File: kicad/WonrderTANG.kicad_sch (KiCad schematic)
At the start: 28 parts, among them CON1 MSX-CONNECTOR, J2 AudioJack3, J3 Conn_02x01, Q1 2N3904, Q2 2N3904, U1 SN74LVC245AN, U2 SN74LVC245AN, U3 SN74LVC245AN, U4 SN74LVC245AN, U5 Tang_Nano_20k, U6 SN74LVC245AN

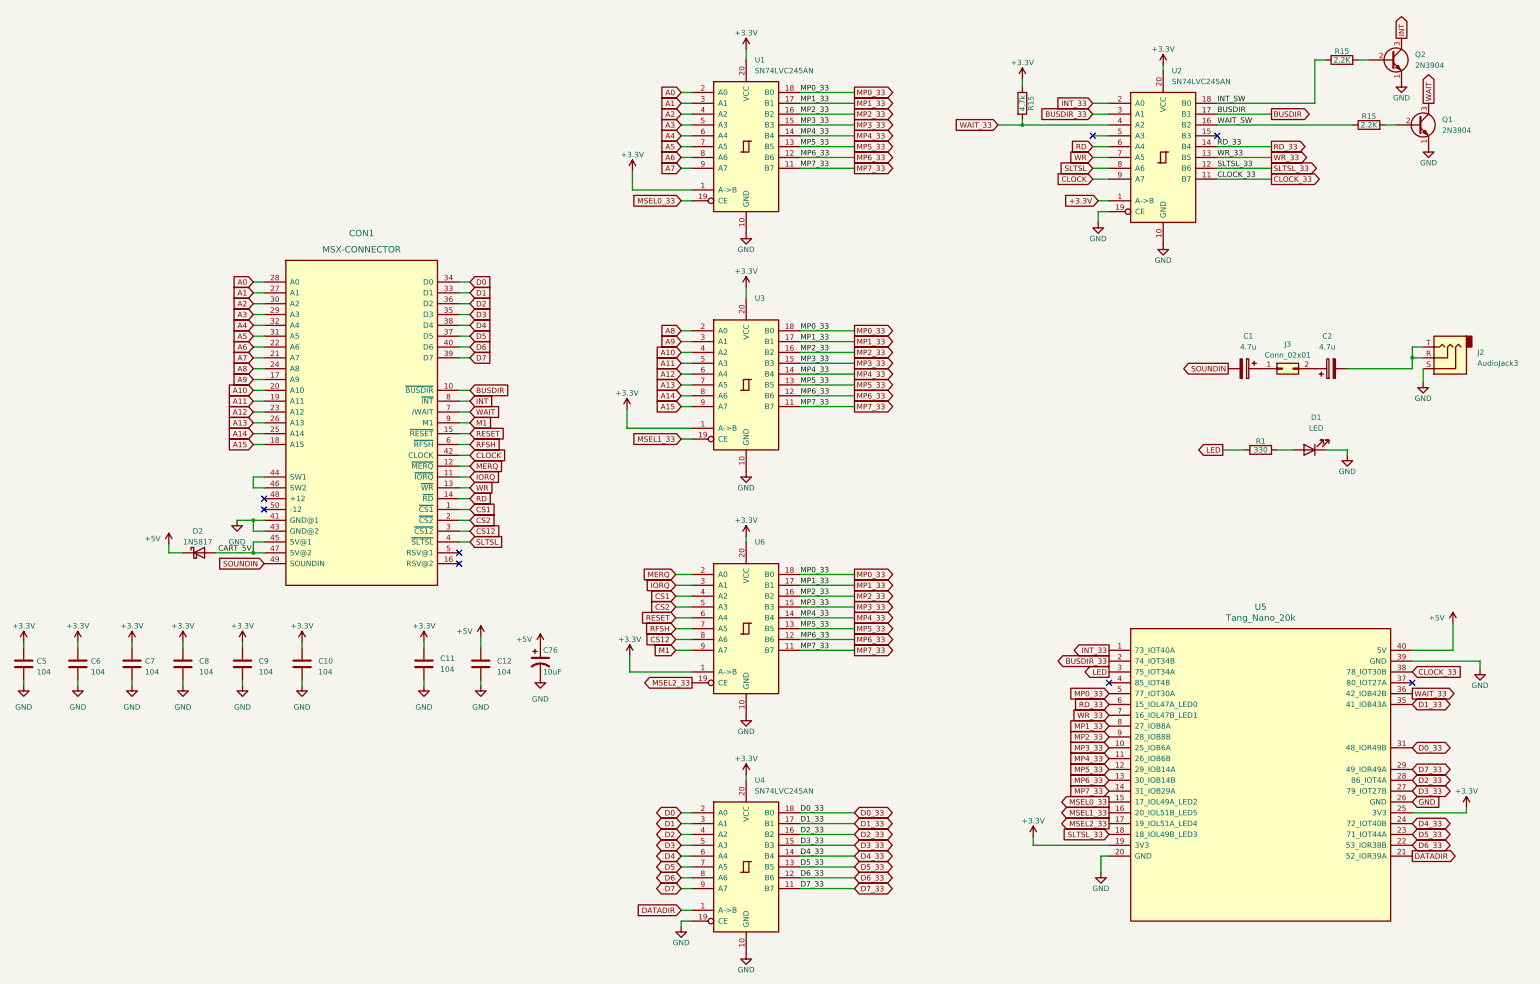
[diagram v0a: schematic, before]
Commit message: Version 2.0b RCC Rev1 - rotated J3 to better fit audio jumper
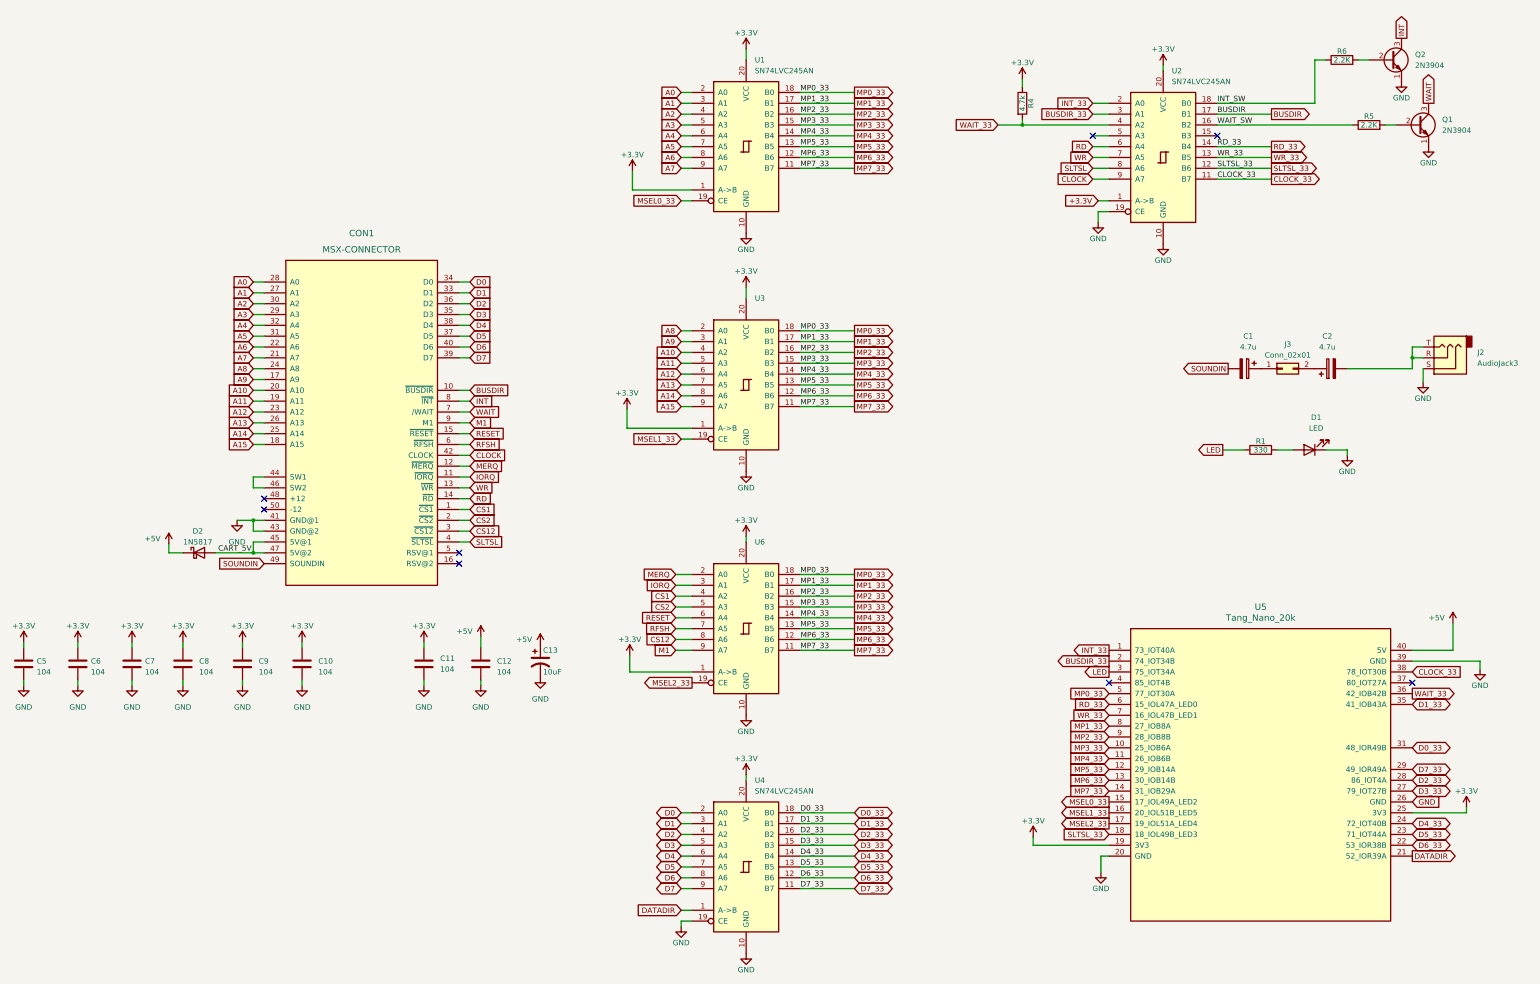
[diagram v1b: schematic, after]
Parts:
- J3: footprint Connector_PinHeader_2.54mm:PinHeader_2x01_P2.54mm_Vertical -> Connector_PinHeader_2.54mm:PinHeader_1x02_P2.54mm_Horizontal
- renumbered C76 to C13, R15 to R4, R15 to R5, R15 to R6
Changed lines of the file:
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@@
 (kicad_sch
-	(version 20231120)
+	(version 20250114)
 	(generator "eeschema")
-	(generator_version "8.0")
+	(generator_version "9.0")
 	(paper "A3")
 	(title_block
 		(title "MSX wonderTANG 2.0")
-		(date "2023-03-01")
+		(date "2025-05-26")
+		(rev "2.0b (RCC Rev 1)")
 	)
 	(junction
@@
 	(label "CART_5V"
 		(at 93.345 153.67 0)
-		(fields_autoplaced yes)
 		(effects
 			(font
@@
 	(label "D0_33"
 		(at 229.87 214.63 0)
-		(fields_autoplaced yes)
 		(effects
 			(font
@@
 	(label "MP5_33"
 		(at 229.87 171.45 0)
-		(fields_autoplaced yes)
 		(effects
 			(font
@@
 	(label "MP0_33"
 		(at 229.87 158.75 0)
-		(fields_autoplaced yes)
 		(effects
 			(font
@@
 	(label "MP2_33"
 		(at 229.87 50.8 0)
-		(fields_autoplaced yes)
 		(effects
 			(font
@@
 	(label "MP5_33"
 		(at 229.87 58.42 0)
-		(fields_autoplaced yes)
 		(effects
 			(font
@@
 	(label "MP6_33"
 		(at 229.9211 116.84 0)
-		(fields_autoplaced yes)
 		(effects
 			(font
@@
 	(label "D5_33"
 		(at 229.87 227.33 0)
-		(fields_autoplaced yes)
 		(effects
 			(font
@@
 	(label "MP5_33"
 		(at 229.87 114.3 0)
-		(fields_autoplaced yes)
 		(effects
 			(font
@@
 	(label "WAIT_SW"
 		(at 327.66 53.34 0)
-		(fields_autoplaced yes)
 		(effects
 			(font
@@
 	(label "D4_33"
 		(at 229.87 224.79 0)
-		(fields_autoplaced yes)
 		(effects
 			(font
@@
 	(label "INT_SW"
 		(at 327.66 48.26 0)
-		(fields_autoplaced yes)
 		(effects
 			(font
@@
 	(label "WR_33"
 		(at 327.66 60.96 0)
-		(fields_autoplaced yes)
 		(effects
 			(font
@@
 	(label "BUSDIR"
 		(at 327.66 50.8 0)
-		(fields_autoplaced yes)
 		(effects
 			(font
@@
 	(label "MP0_33"
 		(at 229.87 101.6 0)
-		(fields_autoplaced yes)
 		(effects
 			(font
@@
 	(label "MP2_33"
 		(at 229.87 163.83 0)
-		(fields_autoplaced yes)
 		(effects
 			(font
@@
 	(label "MP3_33"
 		(at 229.87 109.22 0)
-		(fields_autoplaced yes)
 		(effects
 			(font
@@
 	(label "MP1_33"
 		(at 229.87 161.29 0)
-		(fields_autoplaced yes)
 		(effects
 			(font
@@
 	(label "MP1_33"
 		(at 229.87 48.26 0)
-		(fields_autoplaced yes)
 		(effects
 			(font
@@
 	(label "MP6_33"
 		(at 229.9211 60.96 0)
-		(fields_autoplaced yes)
 		(effects
 			(font
@@
 	(label "RD_33"
 		(at 327.66 58.42 0)
-		(fields_autoplaced yes)
 		(effects
 			(font
@@
 	(label "MP4_33"
 		(at 229.87 55.88 0)
-		(fields_autoplaced yes)
 		(effects
 			(font
@@
 	(label "MP7_33"
 		(at 229.87 63.5 0)
-		(fields_autoplaced yes)
 		(effects
 			(font
@@
 	(label "MP7_33"
 		(at 229.87 176.53 0)
-		(fields_autoplaced yes)
 		(effects
 			(font
@@
 	(label "D6_33"
 		(at 229.87 229.87 0)
-		(fields_autoplaced yes)
 		(effects
 			(font
@@
 	(label "MP4_33"
 		(at 229.87 168.91 0)
-		(fields_autoplaced yes)
 		(effects
 			(font
@@
 	(label "MP3_33"
 		(at 229.87 166.37 0)
-		(fields_autoplaced yes)
 		(effects
 			(font
@@
 	(label "CLOCK_33"
 		(at 327.66 66.04 0)
-		(fields_autoplaced yes)
 		(effects
 			(font
@@
 	(label "D3_33"
 		(at 229.87 222.25 0)
-		(fields_autoplaced yes)
 		(effects
 			(font
@@
 	(label "MP2_33"
 		(at 229.87 106.68 0)
-		(fields_autoplaced yes)
 		(effects
 			(font
@@
 	(label "MP6_33"
 		(at 229.9211 173.99 0)
-		(fields_autoplaced yes)
 		(effects
 			(font
@@
 	(label "MP3_33"
 		(at 229.87 53.34 0)
-		(fields_autoplaced yes)
 		(effects
 			(font
@@
 	(label "MP4_33"
 		(at 229.87 111.76 0)
-		(fields_autoplaced yes)
 		(effects
 			(font
@@
 	(label "D7_33"
 		(at 229.87 232.41 0)
-		(fields_autoplaced yes)
 		(effects
 			(font
@@
 	(label "D2_33"
 		(at 229.87 219.71 0)
-		(fields_autoplaced yes)
 		(effects
 			(font
@@
 	(label "MP0_33"
 		(at 229.87 45.72 0)
-		(fields_autoplaced yes)
 		(effects
 			(font
@@
 	(label "MP7_33"
 		(at 229.87 119.38 0)
-		(fields_autoplaced yes)
 		(effects
 			(font
@@
 	(label "SLTSL_33"
 		(at 327.66 63.5 0)
-		(fields_autoplaced yes)
 		(effects
 			(font
@@
 	(label "MP1_33"
 		(at 229.87 104.14 0)
-		(fields_autoplaced yes)
 		(effects
 			(font
@@
 	(label "D1_33"
 		(at 229.87 217.17 0)
-		(fields_autoplaced yes)
 		(effects
 			(font
@@
 		(on_board yes)
 		(dnp no)
-		(property "Reference" "#PWR091"
+		(property "Reference" "#PWR013"
 			(at 217.17 140.97 0)
 			(effects
@@
 		(on_board yes)
 		(dnp no)
-		(property "Reference" "#PWR091"
+		(property "Reference" "#PWR04"
 			(at 299.72 82.55 0)
 			(effects
@@
 		(on_board yes)
 		(dnp no)
-		(property "Reference" "#PWR091"
+		(property "Reference" "#PWR045"
 			(at 377.19 64.77 0)
 			(effects
@@
 		(on_board yes)
 		(dnp no)
-		(property "Reference" "#PWR093"
+		(property "Reference" "#PWR041"
 			(at 300.355 234.95 0)
 			(effects
@@
 		(on_board yes)
 		(dnp no)
-		(property "Reference" "C76"
+		(property "Reference" "C13"
 			(at 169.545 176.53 0)
 			(effects
@@
 		(on_board yes)
 		(dnp no)
-		(property "Reference" "#PWR091"
+		(property "Reference" "#PWR05"
 			(at 217.17 85.09 0)
 			(effects
@@
 		(on_board yes)
 		(dnp no)
-		(property "Reference" "#PWR091"
+		(property "Reference" "#PWR036"
 			(at 201.93 247.65 0)
 			(effects
@@
 		(on_board yes)
 		(dnp no)
-		(property "Reference" "#PWR093"
+		(property "Reference" "#PWR027"
 			(at 389.255 187.325 0)
 			(effects
@@
 		(on_board yes)
 		(dnp no)
-		(property "Reference" "#PWR091"
+		(property "Reference" "#PWR048"
 			(at 370.84 49.53 0)
 			(effects
@@
 		(on_board yes)
 		(dnp no)
-		(property "Reference" "R15"
+		(property "Reference" "R5"
 			(at 363.22 51.308 90)
 			(effects
@@
 		(on_board yes)
 		(dnp no)
-		(property "Reference" "R15"
+		(property "Reference" "R6"
 			(at 356.87 36.068 90)
 			(effects
@@
 		(on_board yes)
 		(dnp no)
-		(property "Reference" "#PWR091"
+		(property "Reference" "#PWR037"
 			(at 217.17 254 0)
 			(effects
@@
 		(on_board yes)
 		(dnp no)
-		(property "Reference" "#PWR091"
+		(property "Reference" "#PWR010"
 			(at 375.92 120.015 0)
 			(effects
@@
 			)
 		)
-		(property "Footprint" "Connector_PinHeader_2.54mm:PinHeader_2x01_P2.54mm_Vertical"
+		(property "Footprint" "Connector_PinHeader_2.54mm:PinHeader_1x02_P2.54mm_Horizontal"
 			(at 342.9 110.49 0)
 			(effects
@@
 		(on_board yes)
 		(dnp no)
-		(property "Reference" "#PWR091"
+		(property "Reference" "#PWR07"
 			(at 314.96 87.63 0)
 			(effects
@@
 		(on_board yes)
 		(dnp no)
-		(property "Reference" "#PWR091"
+		(property "Reference" "#PWR043"
 			(at 217.17 198.12 0)
 			(effects
@@
 		(on_board yes)
 		(dnp no)
-		(property "Reference" "R15"
+		(property "Reference" "R4"
 			(at 283.972 48.26 90)
 			(effects
@@
 		)
 	)
+	(embedded_fonts no)
 )
